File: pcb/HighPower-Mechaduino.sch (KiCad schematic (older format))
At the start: 53 parts, among them J1 SUPPLY, J2 STEPPER, P1 SWD, P4 CONN_01X04, Q1 SSM3J328R, Q2 BSS138, SW1 B3U-1000P, U1 AS5047D, U2 AP2112K-3.3TRG1, U3 AT24CS64-SSHM, U9 LM75BD

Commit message: Improve BOM
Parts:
- J1: Digi-Key Minimum Quantity (none) -> 1; Digi-Key Part Number (none) -> A98333-ND
- J2: Digi-Key Minimum Quantity (none) -> 1; Digi-Key Part Number (none) -> A98335-ND
- P4: Digi-Key Minimum Quantity (none) -> 1; Digi-Key Part Number (none) -> 455-1706-ND
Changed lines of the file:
@@
 F 1 "STEPPER" H 11131 2451 50  0000 C CNN
 F 2 "Connectors_Terminal_Blocks:TerminalBlock_Pheonix_MPT-2.54mm_4pol" H 11050 1575 50  0001 C CNN
-F 3 "" H 11025 2200 50  0001 C CNN
+F 3 "www.te.com/commerce/DocumentDelivery/DDEController?Action=srchrtrv&DocNm=282834&DocType=Customer+Drawing&DocLang=English" H 11025 2200 50  0001 C CNN
+F 4 "A98335-ND" H 11050 2000 60  0001 C CNN "Digi-Key Part Number"
+F 5 "1" H 11050 2000 60  0001 C CNN "Digi-Key Minimum Quantity"
 	1    11050 2000
 	-1   0    0    -1
@@
 F 1 "SUPPLY" H 1030 4801 50  0000 C CNN
 F 2 "Connectors_Terminal_Blocks:TerminalBlock_Pheonix_MPT-2.54mm_2pol" H 950 4325 50  0001 C CNN
-F 3 "" H 925 4550 50  0001 C CNN
+F 3 "www.te.com/commerce/DocumentDelivery/DDEController?Action=srchrtrv&DocNm=282834&DocType=Customer+Drawing&DocLang=English" H 925 4550 50  0001 C CNN
+F 4 "A98333-ND" H 950 4550 60  0001 C CNN "Digi-Key Part Number"
+F 5 "1" H 950 4550 60  0001 C CNN "Digi-Key Minimum Quantity"
 	1    950  4550
 	1    0    0    1
@@
 F 1 "CONN_01X04" H 11128 4950 50  0000 L CNN
 F 2 "Connectors_JST:JST_PH_B4B-PH-K_04x2.00mm_Straight" H 11127 4904 50  0001 L CNN
-F 3 "" H 11050 5000 50  0000 C CNN
+F 3 "http://www.jst-mfg.com/product/pdf/eng/ePH.pdf" H 11050 5000 50  0001 C CNN
+F 4 "455-1706-ND" H 11050 5000 60  0001 C CNN "Digi-Key Part Number"
+F 5 "1" H 11050 5000 60  0001 C CNN "Digi-Key Minimum Quantity"
 	1    11050 5000
 	1    0    0    -1

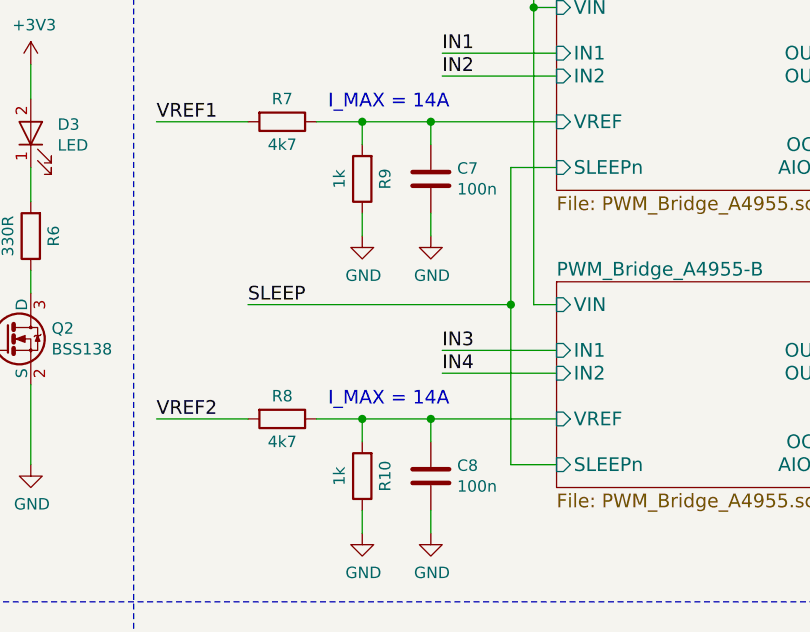
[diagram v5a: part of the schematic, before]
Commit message: Remove connection to SLEEPn Pin
I think we don't have to connect this pin, and if yes we can fix it manually on the prototype

The support of Alegro wasn't very helpful about that topic
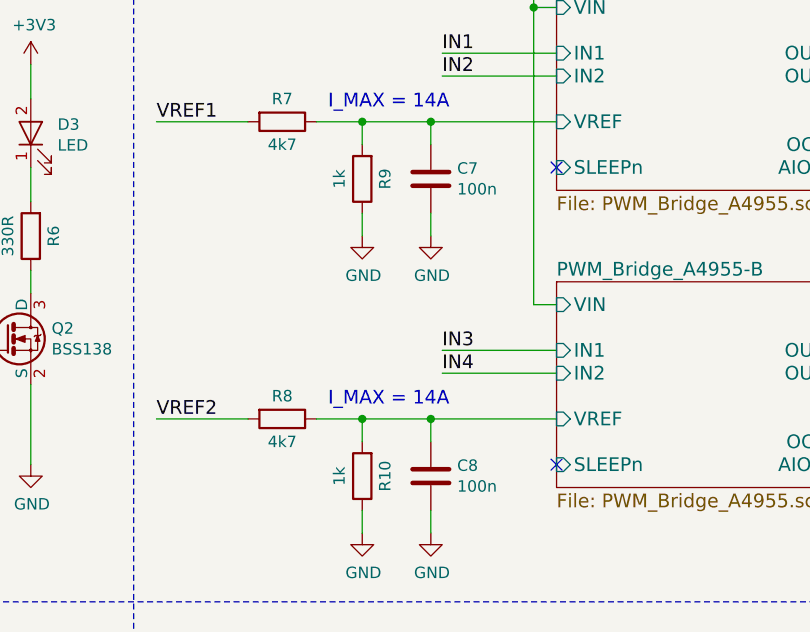
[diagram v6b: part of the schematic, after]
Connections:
- no-connect marks 17 -> 19
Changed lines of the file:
@@
 Text Label 10500 3000 2    60   ~ 0
 AIOUT2
-Text Label 7450 2300 0    60   ~ 0
-SLEEP
 $Comp
 L R R9
@@
 	8800 2600 8300 2600
 Wire Wire Line
-	8600 3000 8800 3000
-Wire Wire Line
-	8600 1700 8600 3000
-Wire Wire Line
-	8600 1700 8800 1700
-Wire Wire Line
 	7850 5150 7450 5150
 Wire Wire Line
@@
 Wire Wire Line
 	10100 3000 10500 3000
-Wire Wire Line
-	8600 2300 7450 2300
-Connection ~ 8600 2300
 Wire Wire Line
 	7950 1900 7950 2000
@@
 Wire Wire Line
 	10250 4850 10850 4850
+NoConn ~ 8800 1700
+NoConn ~ 8800 3000
 $EndSCHEMATC

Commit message: Fix #7
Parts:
- removed C2: 1µ, Capacitors_SMD:C_0603, symbol C
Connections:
- net +3V3: now also C4.2, U1.11 (VDD)
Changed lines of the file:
@@
-$EndComp
-$Comp
-L C C2
-U 1 1 58056280
-P 3450 800
-F 0 "C2" V 3198 800 50  0000 C CNN
-F 1 "1µ" V 3289 800 50  0000 C CNN
-F 2 "Capacitors_SMD:C_0603" H 3488 650 50  0001 C CNN
-F 3 "" H 3450 800 50  0000 C CNN
-F 4 "311-1343-1-ND" H 3450 800 60  0001 C CNN "Digi-Key Part Number"
-F 5 "1" H 3450 800 60  0001 C CNN "Digi-Key Minimum Quantity"
-	1    3450 800
-	0    1    1    0
 $EndComp
 $Comp
@@
 F 3 "" H 4400 850 50  0000 C CNN
 	1    4400 850
-	1    0    0    -1
-$EndComp
-$Comp
-L GND #PWR04
-U 1 1 58057452
-P 3200 850
-F 0 "#PWR04" H 3200 600 50  0001 C CNN
-F 1 "GND" H 3205 677 50  0000 C CNN
-F 2 "" H 3200 850 50  0000 C CNN
-F 3 "" H 3200 850 50  0000 C CNN
-	1    3200 850
 	1    0    0    -1
 $EndComp
@@
 	4400 800  4400 850
 Wire Wire Line
-	3950 800  3800 800
+	3700 800  3950 800
 Wire Wire Line
 	3800 800  3800 900
 Wire Wire Line
 	3700 700  3700 900
-Wire Wire Line
-	3700 800  3600 800
-Wire Wire Line
-	3300 800  3200 800
-Wire Wire Line
-	3200 800  3200 850
 Connection ~ 3700 800
 Wire Wire Line
@@
 NoConn ~ 8800 1700
 NoConn ~ 8800 3000
+Connection ~ 3800 800
 $EndSCHEMATC
